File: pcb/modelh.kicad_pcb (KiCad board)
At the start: 2 copper layers, 150 x 38 mm, 7 parts, among them J2 Conn_01x16, J3 Conn_01x08, J4 Conn_01x04

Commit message: Maybe completed v0.2?
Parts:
- added C1: 1uF, Capacitor_SMD:C_0603_1608Metric, F.Cu at (97.5, 62.2)
- added C2: 22pF, Capacitor_SMD:C_0603_1608Metric, F.Cu at (109.8, 74.2)
- added C3: 22pF, Capacitor_SMD:C_0603_1608Metric, F.Cu at (102.3, 74.2)
- added C4: 1uF, Capacitor_SMD:C_0603_1608Metric, F.Cu at (105.8, 50.5)
- added C5: 10uF, Capacitor_SMD:C_0603_1608Metric, F.Cu at (91.0, 63.0)
- added C6: 1uF, Capacitor_SMD:C_0603_1608Metric, F.Cu at (95.5, 63.0)
- added C7: 0.1uF, Capacitor_SMD:C_0603_1608Metric, F.Cu at (93.3, 63.0)
- added D1: D, Diode_SMD:D_SOD-323, F.Cu at (191.8, 57.2)
- added D2: D, Diode_SMD:D_SOD-323, F.Cu at (189.3, 57.2)
- added D3: D, Diode_SMD:D_SOD-323, F.Cu at (186.8, 57.2)
- added D4: D, Diode_SMD:D_SOD-323, F.Cu at (184.3, 57.2)
- added D5: D, Diode_SMD:D_SOD-323, F.Cu at (181.8, 57.2)
- added D6: D, Diode_SMD:D_SOD-323, F.Cu at (179.3, 57.2)
- added D7: D, Diode_SMD:D_SOD-323, F.Cu at (176.8, 57.2)
- added D8: D, Diode_SMD:D_SOD-323, F.Cu at (174.3, 57.2)
- added J1: USB_B, Connector_USB:USB_B_OST_USB-B1HSxx_Horizontal, F.Cu at (87.5, 57.5)
- added J5: AVR-ISP-6, Connector_IDC:IDC-Header_2x03_P2.54mm_Vertical, F.Cu at (79.7, 67.0)
- added LED1: LED, LED_SMD:LED_0805_2012Metric, F.Cu at (69.8, 51.7)
- added R1: 1k, Resistor_SMD:R_0201_0603Metric, F.Cu at (75.8, 57.5)
- added R2: 10k, Resistor_SMD:R_0201_0603Metric, F.Cu at (103.6, 70.7)
- added R3: 22, Resistor_SMD:R_0201_0603Metric, F.Cu at (98.5, 60.0)
- added R4: 120, Resistor_SMD:R_0201_0603Metric, F.Cu at (204.3, 50.1)
- added R5: 120, Resistor_SMD:R_0201_0603Metric, F.Cu at (204.3, 51.8)
- added R6: 120, Resistor_SMD:R_0201_0603Metric, F.Cu at (204.3, 53.6)
- added R7: 22, Resistor_SMD:R_0201_0603Metric, F.Cu at (98.5, 58.0)
- added SW1: SW_Push, Button_Switch_SMD:SW_SPST_EVPBF, F.Cu at (92.0, 72.5)
- added U1: 74HC595, Package_SO:SOIC-16_3.9x9.9mm_P1.27mm, F.Cu at (181.5, 64.7)
- added U2: ATmega32U4-AU, Package_QFP:TQFP-44_10x10mm_P0.8mm, F.Cu at (106.5, 63.5)
- added Y1: 16MHz, Crystal:Crystal_SMD_3225-4Pin_3.2x2.5mm, F.Cu at (106.0, 74.2)
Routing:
- net +5V: track 0.00 -> 185.3 mm, vias 0 -> 2
- net /led0: track 0.00 -> 106.3 mm
- net /led1: track 0.00 -> 105.7 mm
- net /led2: track 0.00 -> 104.9 mm
- net /row_latch: track 0.00 -> 88.5 mm, vias 0 -> 2
- net /row_clk: track 0.00 -> 86.6 mm, vias 0 -> 2
- net /row_data: track 0.00 -> 86.4 mm, vias 0 -> 2
- net /col15: track 0.00 -> 56.4 mm
- net /col14: track 0.00 -> 52.7 mm
- net /col13: track 0.00 -> 49.0 mm
- net /col11: track 0.00 -> 45.4 mm
- net /col12: track 0.00 -> 44.2 mm
- net /col10: track 0.00 -> 36.0 mm
- net /col9: track 0.00 -> 33.2 mm
- net /col8: track 0.00 -> 30.3 mm
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
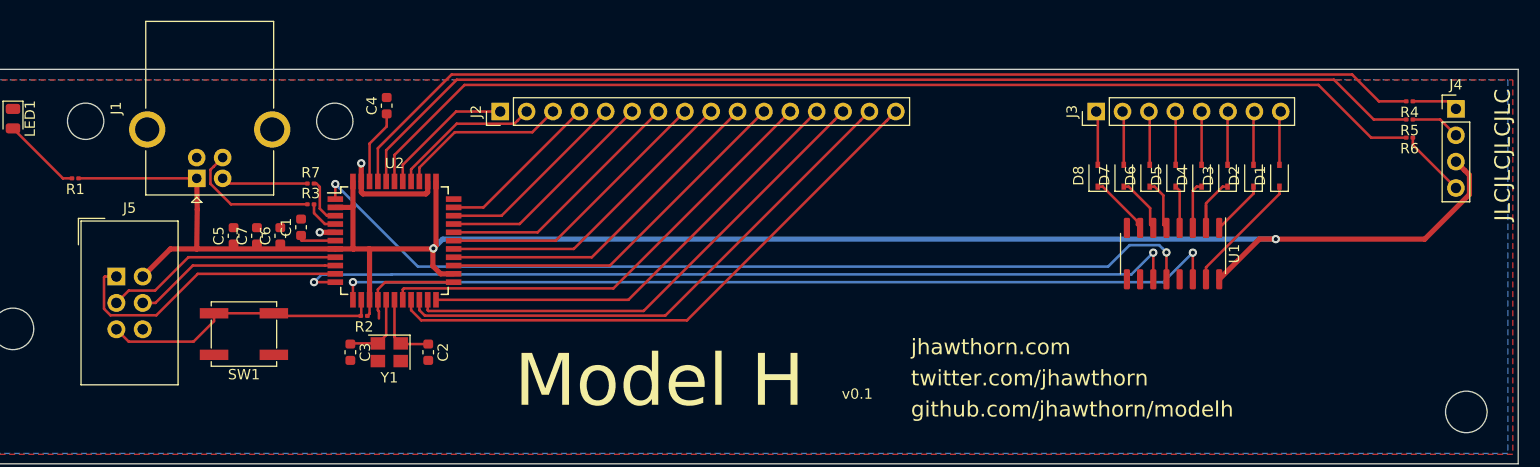
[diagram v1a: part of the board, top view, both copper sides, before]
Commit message: Fix resistor sizes
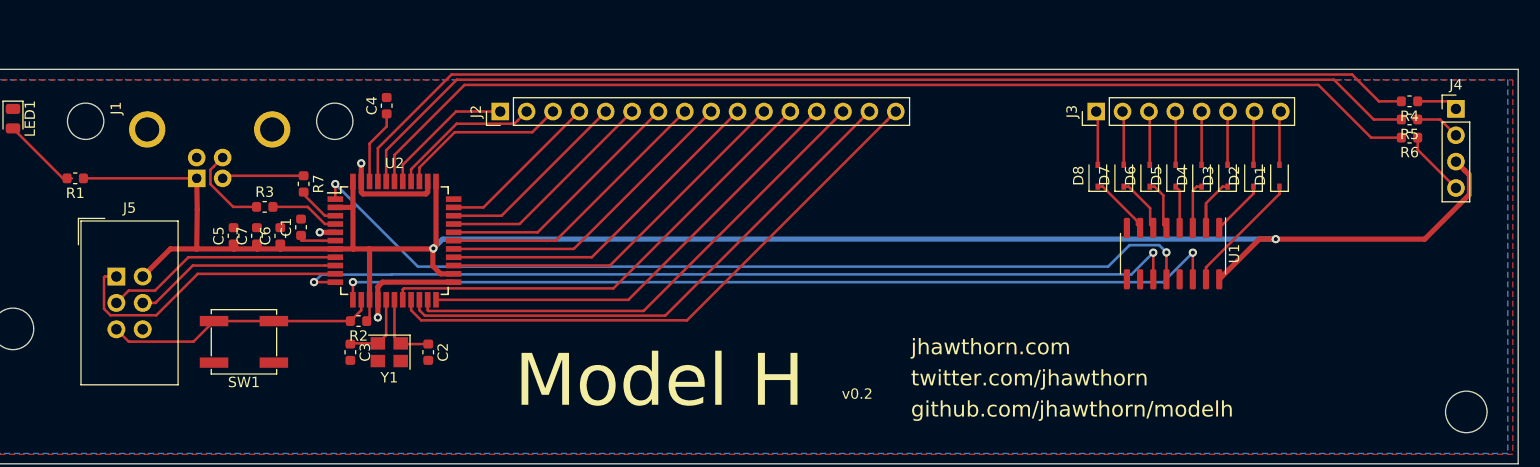
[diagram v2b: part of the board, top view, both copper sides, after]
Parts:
- R1, R2, R3, R4, R5, R6, R7: footprint Resistor_SMD:R_0201_0603Metric -> Resistor_SMD:R_0603_1608Metric
- moved R3 4.44 mm to (94.0, 60.2)
- moved SW1 0.75 mm to (92.0, 73.2)
- moved R2 0.73 mm to (103.1, 71.2)
- moved R7 0.68 mm to (97.8, 58.0), turned to 270 degrees
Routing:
- net Net-(J1-Pad3): track 13.2 -> 8.39 mm
- net /D+: track 3.33 -> 6.70 mm
- net /RST: track 27.3 -> 25.6 mm
- net +5V: track 185.3 -> 186.9 mm
- net GND: vias 2 -> 3
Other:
- board text added: "v0.2"
- board text removed: "JLCJLCJLCJLC"
- board text removed: "v0.1"

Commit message: More work
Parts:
- added C8: 0.1uF, Capacitor_SMD:C_0603_1608Metric, F.Cu at (188.0, 67.0)
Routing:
- net +5V: track 186.9 -> 201.7 mm
- net GND: vias 3 -> 5

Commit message: PCB updates
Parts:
- Y1: value 16MHz -> Crystal_GND24
- moved C3 2.06 mm to (104.3, 73.7), turned to 90 degrees
- moved Y1 1.82 mm to (107.8, 73.7), turned to 0 degrees
- moved C2 1.35 mm to (111.0, 73.7)
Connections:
- Y1 pad 1: Net-(C2-Pad1) -> Net-(C3-Pad1)
- Y1 pad 2: Net-(C3-Pad1) -> GND
- Y1 pad 3: (no net) -> Net-(C2-Pad1)
- Y1 pad 4: (no net) -> GND
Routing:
- net Net-(C3-Pad1): track 7.21 -> 9.21 mm

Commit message: WIP
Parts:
- removed D2, D3, D4, D5, D6, D7, D8: D, Diode_SMD:D_SOD-323
- removed the R7 at (97.8, 58.0)
- added C10: 100 nF, Capacitor_SMD:C_0402_1005Metric, F.Cu at (101.9, 60.8)
- added C11: 100 nF, Capacitor_SMD:C_0402_1005Metric, F.Cu at (113.5, 66.6)
- added C12: 100 nF, Capacitor_SMD:C_0402_1005Metric, F.Cu at (108.0, 69.5)
- added C13: 100 nF, Capacitor_SMD:C_0402_1005Metric, F.Cu at (111.0, 56.7)
- added C14: 100 nF, Capacitor_SMD:C_0402_1005Metric, F.Cu at (106.0, 69.5)
- added C9: 100nF, Capacitor_SMD:C_0603_1608Metric, F.Cu at (108.2, 75.3)
- added J6: Conn_02x05_Odd_Even, Connector_IDC:IDC-Header_2x05_P2.54mm_Vertical, F.Cu at (79.8, 80.1)
- added LED2: LED, LED_SMD:LED_0805_2012Metric, F.Cu at (104.3, 73.0)
- added R10: 100k, Resistor_SMD:R_0603_1608Metric, F.Cu at (99.3, 66.4)
- added R11: 1.5k, Resistor_SMD:R_0603_1608Metric, F.Cu at (77.1, 60.0)
- added R4: 22, Resistor_SMD:R_0603_1608Metric, F.Cu at (98.8, 56.7)
- added R5: 100k, Resistor_SMD:R_0603_1608Metric, F.Cu at (99.3, 67.9)
- added R6: 1M, Resistor_SMD:R_0603_1608Metric, F.Cu at (119.5, 70.4)
- added Y2: 32.768KHz, Crystal:Crystal_SMD_3215-2Pin_3.2x1.5mm, F.Cu at (111.8, 72.0)
- C1: value 1uF -> 100uF
- C2: value 22pF -> 100nF; footprint Capacitor_SMD:C_0603_1608Metric -> Capacitor_SMD:C_0402_1005Metric
- C3: value 22pF -> 330uF
- C4: value 1uF -> 100nF; footprint Capacitor_SMD:C_0603_1608Metric -> Capacitor_SMD:C_0402_1005Metric
- C5: value 10uF -> 20pF
- C6: value 1uF -> 20pF
- C7, C8: value 0.1uF -> 20pF
- D1: value D -> B5819W; footprint Diode_SMD:D_SOD-323 -> Diode_SMD:D_SOD-123
- J5: value AVR-ISP-6 -> Conn_02x03_Odd_Even; footprint Connector_IDC:IDC-Header_2x03_P2.54mm_Vertical -> Connector_PinHeader_2.54mm:PinHeader_2x03_P2.54mm_Vertical
- R1: value 1k -> 330
- R2: value 10k -> 330
- U1: value 74HC595 -> STM32F103C8Tx; footprint Package_SO:SOIC-16_3.9x9.9mm_P1.27mm -> Package_QFP:LQFP-48_7x7mm_P0.5mm
- U2: value ATmega32U4-AU -> AMS1117-3.3; footprint Package_QFP:TQFP-44_10x10mm_P0.8mm -> Package_TO_SOT_SMD:SOT-223-3_TabPin2
- Y1: value Crystal_GND24 -> 8MHz; footprint Crystal:Crystal_SMD_3225-4Pin_3.2x2.5mm -> Crystal:Crystal_SMD_5032-2Pin_5.0x3.2mm
- moved D1 106.0 mm to (85.9, 60.6), turned to 0 degrees
- moved C8 75.5 mm to (113.0, 75.2)
- moved U1 73.3 mm to (108.3, 63.0), turned to 135 degrees
- moved C2 35.1 mm to (77.6, 63.2), turned to 180 degrees
- moved C5 28.4 mm to (117.0, 74.5), turned to 0 degrees
- moved U2 24.3 mm to (82.5, 67.2), turned to 270 degrees
- moved C4 24.0 mm to (88.5, 67.1)
- moved C6 21.5 mm to (116.8, 66.5), turned to 0 degrees
- moved C7 21.1 mm to (110.5, 75.2), turned to 270 degrees
- moved C1 20.4 mm to (77.1, 61.5), turned to 180 degrees
- moved C3 18.3 mm to (87.2, 67.2)
- moved J5 16.2 mm to (95.6, 70.3), turned to 180 degrees
- moved SW1 11.7 mm to (101.9, 79.6)
- moved Y1 9.57 mm to (116.8, 70.5), turned to 90 degrees
- moved R3 5.06 mm to (98.8, 58.5)
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- renumbered R4 to R7, R5 to R8, R6 to R9
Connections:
- C1 pad 1: Net-(C1-Pad1) -> +5V
- C2 pad 1: Net-(C2-Pad1) -> +5V
- C3 pad 1: Net-(C3-Pad1) -> +3V3
- C4 pad 1: Net-(C4-Pad1) -> +3V3
- C5 pad 1: +5V -> /OSC8IN
- C6 pad 1: +5V -> /OSC8OUT
- C7 pad 1: +5V -> /OSC32IN
- C8 pad 1: +5V -> /OSC32OUT
- D1 pad 1: Net-(D1-Pad1) -> +5V
- D1 pad 2: /row7 -> Net-(D1-Pad2)
- J1 pad 1: +5V -> Net-(D1-Pad2)
- J4 pad 3: +5V -> +3V3
- J5 pad 1: /MISO -> +3V3
- J5 pad 2: +5V -> +3V3
- J5 pad 3: /SCK -> Net-(J5-Pad3)
- J5 pad 4: /MOSI -> Net-(J5-Pad4)
- J5 pad 5: /RST -> GND
- R1 pad 1: +5V -> +3V3
- R2 pad 1: +5V -> /STATUSLED
- R2 pad 2: /RST -> Net-(LED2-Pad2)
- SW1 pad 2: /RST -> /nRST
- U1 pad 1: Net-(D2-Pad1) -> +3V3
- U1 pad 10: +5V -> /row5
- U1 pad 11: /row_clk -> /row7
- U1 pad 12: /row_latch -> /row6
- U1 pad 13: GND -> /col15
- U1 pad 14: /row_data -> /col14
- U1 pad 15: Net-(D1-Pad1) -> /col13
- U1 pad 16: +5V -> /col12
- U1 pad 2: Net-(D3-Pad1) -> /STATUSLED
- U1 pad 3: Net-(D4-Pad1) -> /OSC32IN
- U1 pad 4: Net-(D5-Pad1) -> /OSC32OUT
- U1 pad 5: Net-(D6-Pad1) -> /OSC8IN
- U1 pad 6: Net-(D7-Pad1) -> /OSC8OUT
- U1 pad 7: Net-(D8-Pad1) -> /nRST
- U1 pad 9: (no net) -> +3V3
- U2 pad 1: /row_latch -> GND
- U2 pad 2: +5V -> +3V3
- U2 pad 3: /D- -> +5V
- Y1 pad 1: Net-(C3-Pad1) -> /OSC8IN
- Y1 pad 2: GND -> /OSC8OUT
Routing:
- net +5V: track 201.7 -> 13.5 mm, vias 2 -> 0
- net +3V3: track 0.00 -> 129.3 mm, vias 0 -> 2
- net /led0: track 105.8 -> 0.00 mm, vias 0 -> 1
- net /led1: track 105.2 -> 0.00 mm, vias 0 -> 1
- net /led2: track 104.4 -> 0.00 mm, vias 0 -> 1
- net /row_latch: track 88.5 -> 0.00 mm, vias 2 -> 0
- net /row_clk: track 86.6 -> 0.00 mm, vias 2 -> 0
- net /row_data: track 86.4 -> 0.00 mm, vias 2 -> 0
- net /row4: track 5.14 -> 88.7 mm, vias 0 -> 2
- net /row3: track 5.15 -> 85.7 mm, vias 0 -> 2
- net /row7: track 5.19 -> 85.1 mm
- net /row2: track 5.17 -> 82.8 mm, vias 0 -> 2
- net /row5: track 5.15 -> 81.7 mm
- net /row6: track 5.17 -> 81.6 mm
- net /row1: track 5.18 -> 79.5 mm, vias 0 -> 2
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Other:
- board text added: "columns"
- board text added: "rows"
- board text added: "v1.0a"
- board text removed: "v0.2"

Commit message: Fix DRC
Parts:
- moved D1 0.85 mm to (85.9, 61.5)
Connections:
- net /BOOT0 renamed BOOT0
- net /BOOT1 renamed BOOT1
- net /D+ renamed D+
- net /D- renamed D-
- net /OSC32IN renamed OSC32IN
- net /OSC32OUT renamed OSC32OUT
- net /OSC8IN renamed OSC8IN
- net /OSC8OUT renamed OSC8OUT
- net /STATUSLED renamed STATUSLED
- net /SWCLK renamed SWCLK
- net /SWDIO renamed SWDIO
- net /col0 renamed col0
- net /col1 renamed col1
- net /col10 renamed col10
- net /col11 renamed col11
- net /col12 renamed col12
- net /col13 renamed col13
- net /col14 renamed col14
- net /col15 renamed col15
- net /col2 renamed col2
- net /col3 renamed col3
- net /col4 renamed col4
- net /col5 renamed col5
- net /col6 renamed col6
- net /col7 renamed col7
- net /col8 renamed col8
- net /col9 renamed col9
- net /led0 renamed led0
- net /led1 renamed led1
- net /led2 renamed led2
- net /nRST renamed nRST
- net /row0 renamed row0
- net /row1 renamed row1
- net /row2 renamed row2
- net /row3 renamed row3
- net /row4 renamed row4
- net /row5 renamed row5
- net /row6 renamed row6
- net /row7 renamed row7
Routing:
- net Net-(D1-Pad2): track 3.17 -> 4.02 mm
- net led2: vias 1 -> 0
- net led1: vias 1 -> 0
- net led0: vias 1 -> 0
- net GND: vias 14 -> 12
- net /led2: vias 0 -> 1
- net /led1: vias 0 -> 1
- net /led0: vias 0 -> 1
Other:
- net class Default: clearance 0.2 -> 0.15; trace_width 0.25 -> 0.2
- rule trace_clearance: 0.2 -> 0.15

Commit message: WIP
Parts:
- moved R7 9.90 mm to (201.2, 59.5)
- moved R8 9.90 mm to (201.2, 61.2)
- moved R9 9.90 mm to (201.2, 63.0)
- moved J3 2.50 mm to (174.1, 53.6)
- moved LED2 2.00 mm to (102.3, 73.0)
- moved R2 2.00 mm to (105.5, 72.8)
- moved C5 1.30 mm to (117.0, 75.8)
- moved C6 1.30 mm to (116.8, 67.8)
- moved Y1 1.30 mm to (116.8, 71.8)
- moved R6 1.30 mm to (119.5, 71.7)
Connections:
- U1 pad 43: led0 -> led2
- U1 pad 46: led2 -> led0
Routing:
- net +3V3: track 129.3 -> 237.4 mm
- net led1: track 0.00 -> 98.4 mm, vias 0 -> 2
- net led0: track 0.00 -> 98.1 mm, vias 0 -> 2
- net led2: track 0.00 -> 98.0 mm, vias 0 -> 2
- net nRST: track 19.1 -> 33.1 mm, vias 0 -> 2
- net Net-(J4-Pad1): track 0.00 -> 12.3 mm
- net Net-(J4-Pad2): track 0.00 -> 10.9 mm
- net Net-(J4-Pad4): track 0.00 -> 8.67 mm
- net STATUSLED: track 3.58 -> 7.39 mm
- net row0: track 76.5 -> 74.8 mm
- net Net-(LED2-Pad2): track 0.00 -> 1.63 mm
- net OSC8IN: track 14.1 -> 15.5 mm
- net row7: track 85.1 -> 84.1 mm
- net row6: track 81.6 -> 80.5 mm
- net row5: track 81.7 -> 80.7 mm
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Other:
- net class Default: clearance 0.15 -> 0.2; trace_width 0.2 -> 0.25
- rule trace_clearance: 0.15 -> 0.2
- board text added: "Boot"
- board text added: "Columns"
- board text added: "Debug"
- board text added: "LEDs"
- board text added: "Reset"
- board text added: "Rows"
- board text added: "https://modelh.club"
- board text removed: "columns"
- board text removed: "github.com/jhawthorn/modelh"
- board text removed: "jhawthorn.com"
- board text removed: "rows"
- board text removed: "twitter.com/jhawthorn"

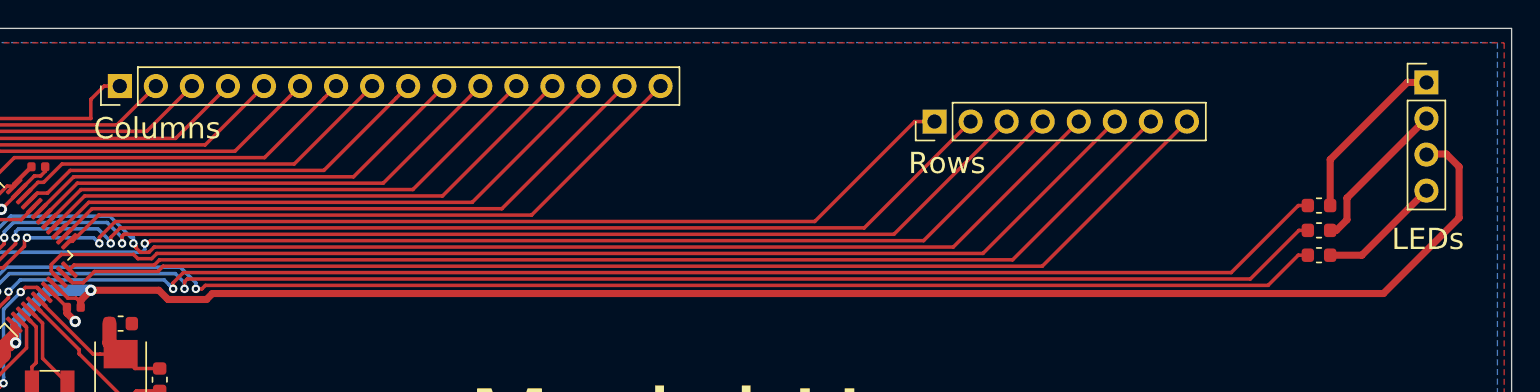
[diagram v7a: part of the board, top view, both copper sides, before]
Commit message: Attempt at supporting 12 pin keyboards
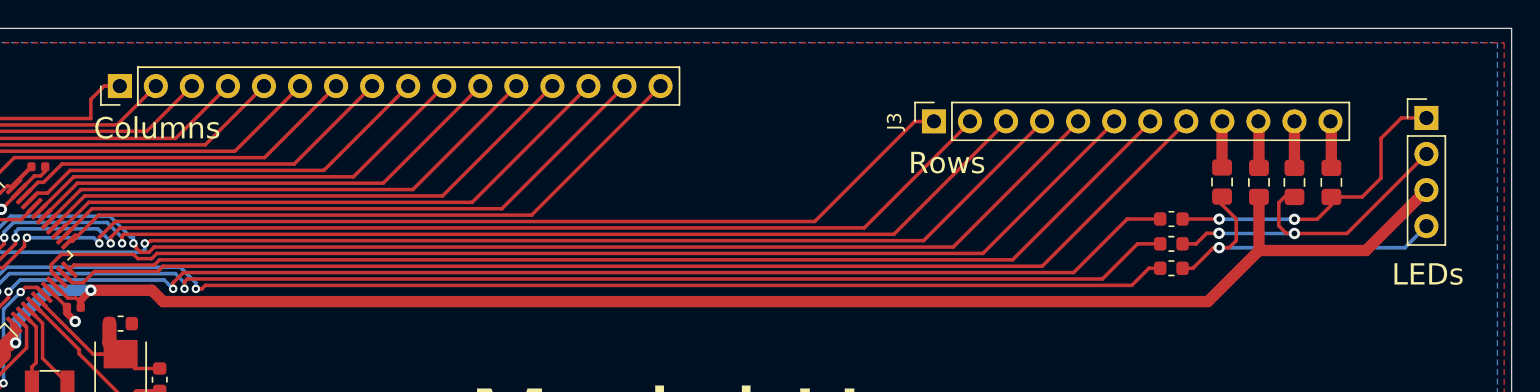
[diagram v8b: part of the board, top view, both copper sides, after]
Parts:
- added R12: 0, Resistor_SMD:R_0805_2012Metric_Pad1.15x1.40mm_HandSolder, F.Cu at (194.4, 57.8)
- added R13: 0, Resistor_SMD:R_0805_2012Metric_Pad1.15x1.40mm_HandSolder, F.Cu at (197.0, 57.8)
- added R14: 0, Resistor_SMD:R_0805_2012Metric_Pad1.15x1.40mm_HandSolder, F.Cu at (199.5, 57.8)
- added R15: 0, Resistor_SMD:R_0805_2012Metric_Pad1.15x1.40mm_HandSolder, F.Cu at (202.1, 57.8)
- J3: value Conn_01x08 -> Conn_01x12; footprint Connector_PinHeader_2.54mm:PinHeader_1x08_P2.54mm_Vertical -> Connector_PinSocket_2.54mm:PinSocket_1x12_P2.54mm_Vertical
- moved R7 10.4 mm to (190.8, 60.4)
- moved R8 10.4 mm to (190.8, 62.2)
- moved R9 10.4 mm to (190.8, 63.9)
- moved J4 2.50 mm to (208.8, 53.3)
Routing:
- net Net-(J4-Pad4): track 8.67 -> 23.3 mm, vias 0 -> 1
- net Net-(J4-Pad2): track 10.9 -> 24.0 mm, vias 0 -> 2
- net led1: track 98.4 -> 87.7 mm
- net led0: track 98.1 -> 87.3 mm
- net led2: track 98.0 -> 87.2 mm
- net Net-(J4-Pad1): track 12.3 -> 22.1 mm, vias 0 -> 2
- net +3V3: track 237.4 -> 233.5 mm
- net Net-(J3-Pad12): track 0.00 -> 3.30 mm
- net Net-(J3-Pad10): track 0.00 -> 3.29 mm
- net Net-(J3-Pad11): track 0.00 -> 3.27 mm
- net Net-(J3-Pad9): track 0.00 -> 3.26 mm
